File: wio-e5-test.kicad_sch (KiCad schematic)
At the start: 31 parts, among them J1 JST PH 2.0, J3 Cortex, J4 Conn_01x13_Pin, J5 SMA, J6 Conn_01x04_Qwiic, J7 Conn_01x09_Pin, SW1 PTS815, SW2 PTS815, SW3 PTS815, U1 MIC5318-3.3YD5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

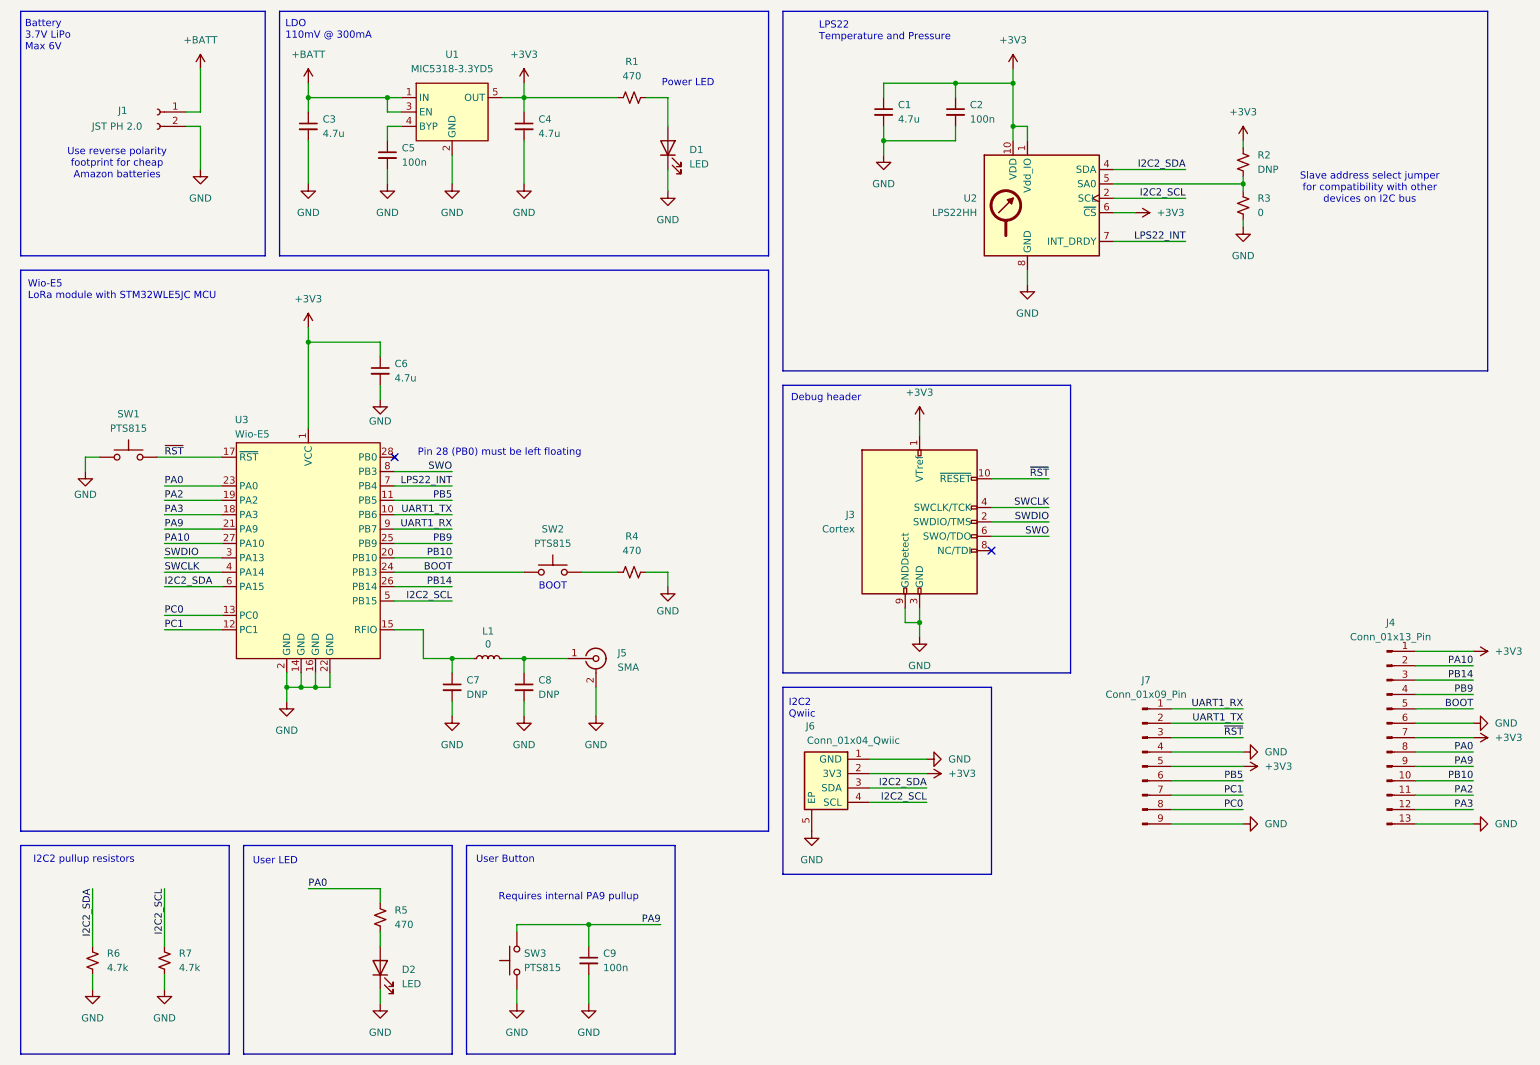
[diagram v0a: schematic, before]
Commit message: Move schematic stuff around
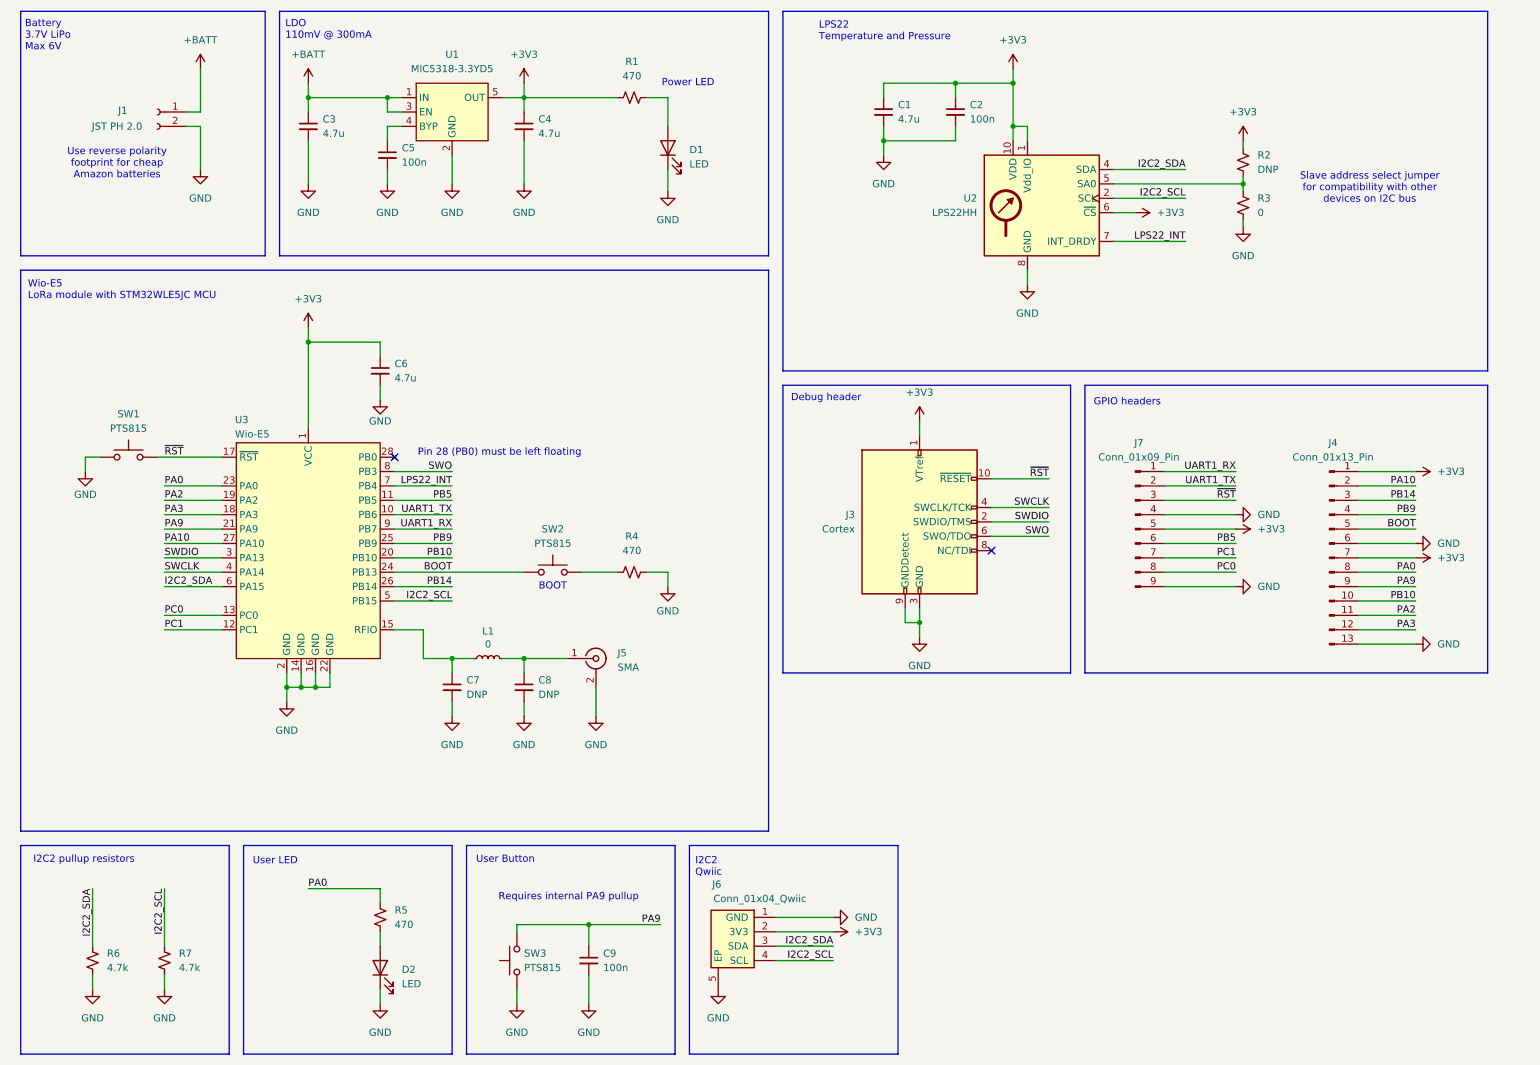
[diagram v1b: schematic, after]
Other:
- note added: "GPIO headers"
- moved on the sheet: J4, J6, J7
